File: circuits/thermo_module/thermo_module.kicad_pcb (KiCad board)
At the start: 2 copper layers, 32.4 x 39.4 mm, 16 parts, among them IC3 LM285Z-1.2, IC4 TMP36

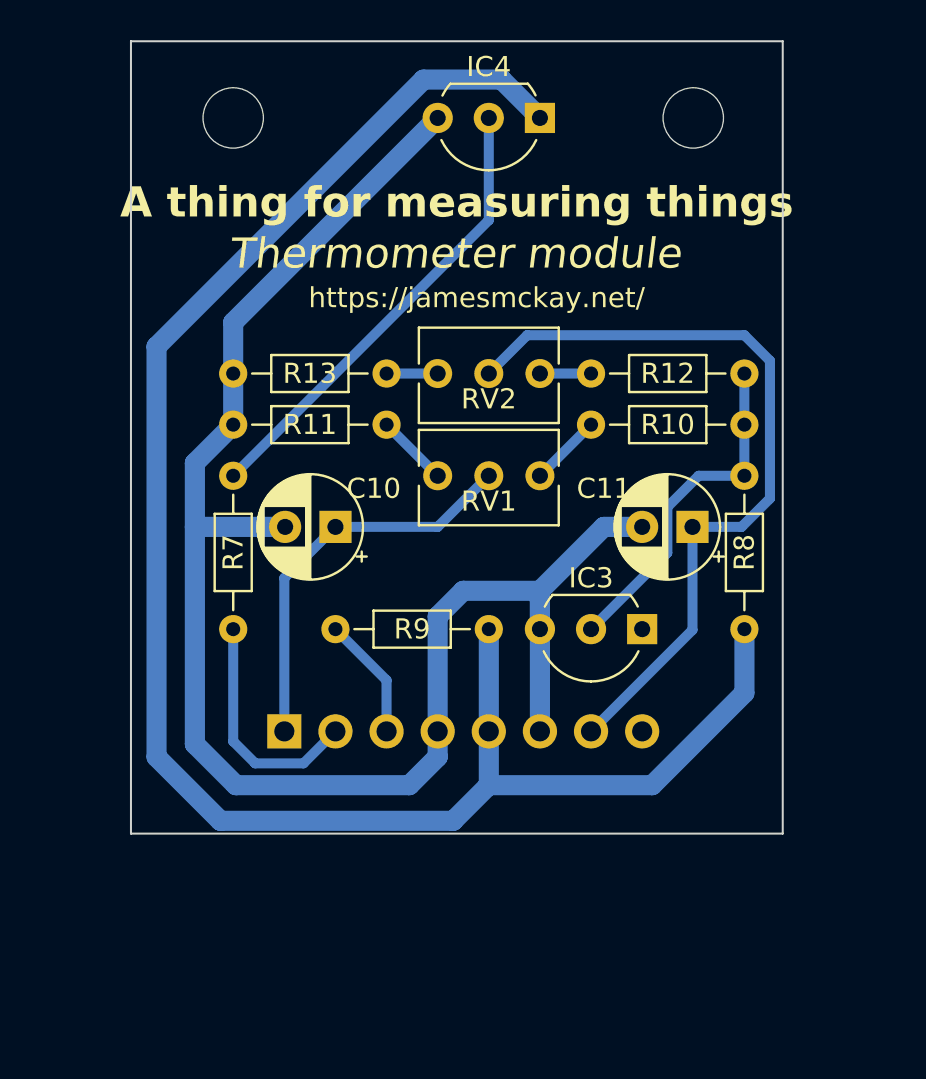
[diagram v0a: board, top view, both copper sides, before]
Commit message: Redesign thermo module to make it work
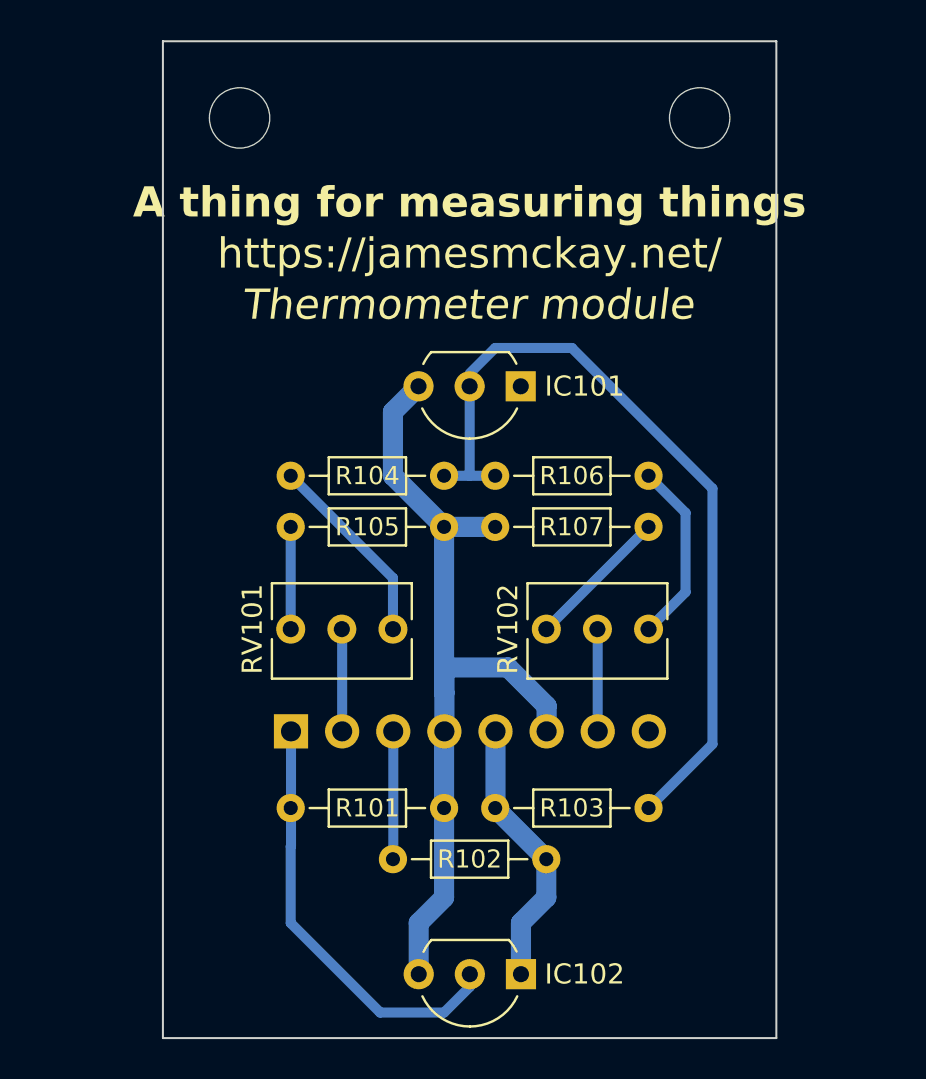
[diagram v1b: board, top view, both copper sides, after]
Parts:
- removed C10, C11: 1uF, Capacitor_THT:CP_Radial_D5.0mm_P2.50mm
- removed J5: ~, Connector_PinHeader_2.54mm:PinHeader_1x08_P2.54mm_Vertical
- removed R7: 33k, Resistor_THT:R_Axial_DIN0204_L3.6mm_D1.6mm_P7.62mm_Horizontal
- added J101: ~, Connector_PinHeader_2.54mm:PinHeader_1x08_P2.54mm_Vertical, B.Cu at (144.2, 79.4)
- added R101: 47k, Resistor_THT:R_Axial_DIN0204_L3.6mm_D1.6mm_P7.62mm_Horizontal, F.Cu at (151.8, 83.2)
- R103: renamed from R8; value 150k -> 75k
- R104: renamed from R10; value 100k -> 51k
- R105: renamed from R11; value 68k -> 33k
- R106: renamed from R12; value 20k -> 10k
- R107: renamed from R13; value 100k -> 51k
- moved IC102 42.6 mm to (155.6, 91.4)
- moved R103 15.2 mm to (154.3, 83.2), turned to 0 degrees
- moved R104 15.1 mm to (151.8, 66.7)
- moved R107 15.1 mm to (161.9, 69.2)
- moved RV102 13.8 mm to (161.9, 74.3)
- moved IC101 13.5 mm to (155.6, 62.2)
- moved R106 13.4 mm to (154.3, 66.7), turned to 0 degrees
- moved R102 11.8 mm to (156.8, 85.7)
- moved RV101 10.6 mm to (149.2, 74.3)
- moved R105 6.96 mm to (144.1, 69.2), turned to 0 degrees
- moved REF** 0.32 mm to (141.6, 48.9)
- moved REF** 0.32 mm to (164.5, 48.9)
- renumbered IC3 to IC101, IC4 to IC102, R9 to R102, RV1 to RV101, RV2 to RV102
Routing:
- net Net-(IC102-+V_{S}): track 89.8 -> 13.6 mm
- net Net-(IC101-A): track 81.5 -> 42.2 mm
- net Net-(J101-Pin_7): track 38.8 -> 5.06 mm
- net Net-(IC101-K): track 16.9 -> 39.7 mm
- net Net-(J101-Pin_2): track 19.9 -> 5.06 mm
- net Net-(J5-Pin_2): track 11.8 -> 0.00 mm
- net Net-(R106-Pad2): track 2.54 -> 9.14 mm
- net Net-(R104-Pad2): track 3.59 -> 9.72 mm
- net Net-(R107-Pad1): track 2.54 -> 7.18 mm
- net Net-(IC102-V_{OUT}): track 23.0 -> 21.4 mm
- net Net-(R105-Pad1): track 3.59 -> 5.08 mm
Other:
- board size 32.4 x 39.4 mm -> 30.5 x 49.5 mm

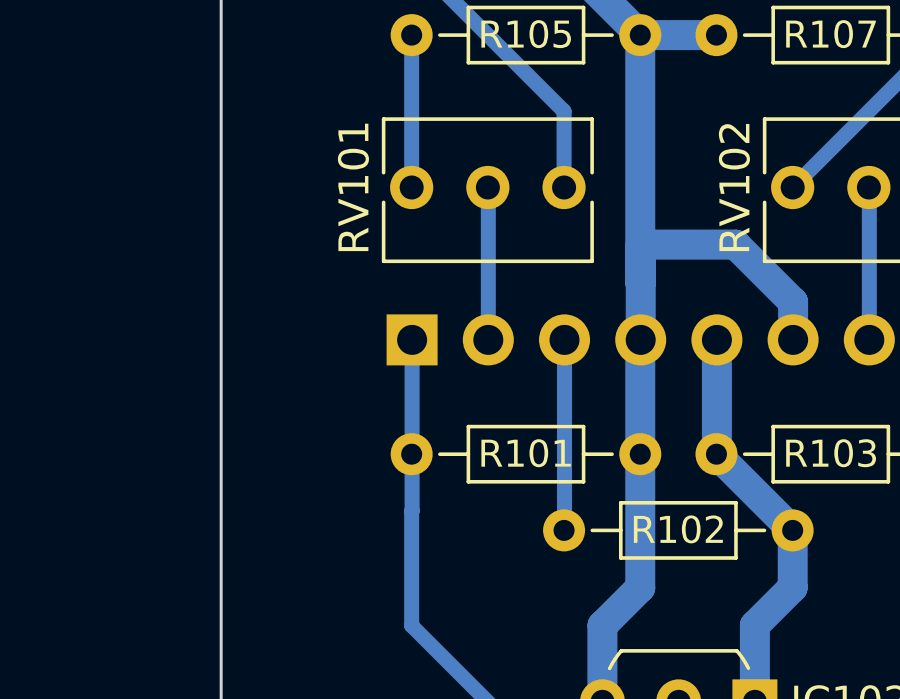
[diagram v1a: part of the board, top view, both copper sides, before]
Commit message: Fix for input pins the wrong way round
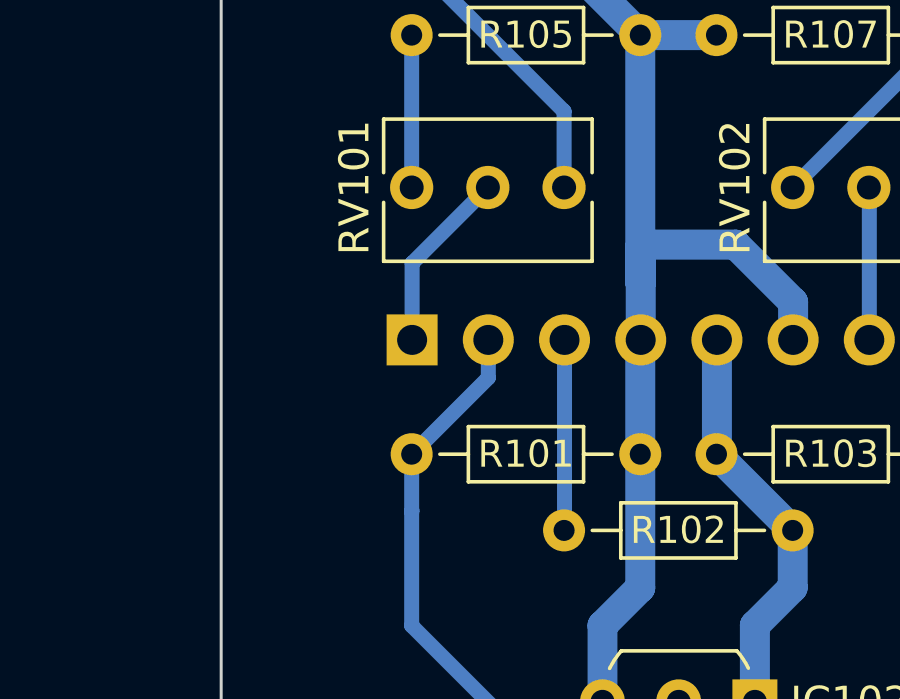
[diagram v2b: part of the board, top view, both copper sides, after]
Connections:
- J101 pad 1: Net-(IC102-V_{OUT}) -> Net-(J101-Pin_1)
- J101 pad 2: Net-(J101-Pin_2) -> Net-(IC102-V_{OUT})
- RV101 pad 2: Net-(J101-Pin_2) -> Net-(J101-Pin_1)
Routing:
- net Net-(J101-Pin_1): track 0.00 -> 6.13 mm
- net Net-(J101-Pin_2): track 5.06 -> 0.00 mm
- net Net-(IC102-V_{OUT}): track 21.4 -> 22.5 mm
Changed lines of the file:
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@@
       (disableapertmacros false)
       (usegerberextensions true)
-      (usegerberattributes true)
-      (usegerberadvancedattributes true)
+      (usegerberattributes false)
+      (usegerberadvancedattributes false)
       (creategerberjobfile false)
       (dashed_line_dash_ratio 12.000000)
@@
       (psa4output false)
       (plotreference true)
-      (plotvalue true)
+      (plotvalue false)
       (plotinvisibletext false)
       (sketchpadsonfab false)
@@
   (net 3 "Net-(IC102-+V_{S})")
   (net 4 "Net-(IC102-V_{OUT})")
-  (net 5 "Net-(J101-Pin_2)")
+  (net 5 "Net-(J101-Pin_1)")
   (net 6 "Net-(J101-Pin_3)")
   (net 7 "Net-(J101-Pin_7)")
@@
       (net 9 "Net-(R104-Pad2)") (pinfunction "1") (pintype "passive"))
     (pad "2" thru_hole circle (at -2.54 0) (size 1.44 1.44) (drill 0.8) (layers "*.Cu" "*.Mask")
-      (net 5 "Net-(J101-Pin_2)") (pinfunction "2") (pintype "passive"))
+      (net 5 "Net-(J101-Pin_1)") (pinfunction "2") (pintype "passive"))
     (pad "3" thru_hole circle (at -5.08 0) (size 1.44 1.44) (drill 0.8) (layers "*.Cu" "*.Mask")
       (net 10 "Net-(R105-Pad1)") (pinfunction "3") (pintype "passive"))
@@
       (stroke (width 0.1) (type solid)) (layer "B.Fab"))
     (pad "1" thru_hole rect (at 0 0 270) (size 1.7 1.7) (drill 1) (layers "*.Cu" "*.Mask")
-      (net 4 "Net-(IC102-V_{OUT})") (pinfunction "Pin_1") (pintype "passive"))
+      (net 5 "Net-(J101-Pin_1)") (pinfunction "Pin_1") (pintype "passive"))
     (pad "2" thru_hole oval (at 0 -2.54 270) (size 1.7 1.7) (drill 1) (layers "*.Cu" "*.Mask")
-      (net 5 "Net-(J101-Pin_2)") (pinfunction "Pin_2") (pintype "passive"))
+      (net 4 "Net-(IC102-V_{OUT})") (pinfunction "Pin_2") (pintype "passive"))
     (pad "3" thru_hole oval (at 0 -5.08 270) (size 1.7 1.7) (drill 1) (layers "*.Cu" "*.Mask")
       (net 6 "Net-(J101-Pin_3)") (pinfunction "Pin_3") (pintype "passive"))
@@
   (segment (start 155.585 91.44) (end 155.585 88.89) (width 1) (layer "B.Cu") (net 3))
   (segment (start 156.845 87.63) (end 156.845 85.725) (width 1) (layer "B.Cu") (net 3))
+  (segment (start 144.145 85.09) (end 144.145 83.185) (width 0.5) (layer "B.Cu") (net 4))
+  (segment (start 146.7 80.6375) (end 146.7 79.375) (width 0.5) (layer "B.Cu") (net 4))
   (segment (start 144.145 88.9) (end 148.59 93.345) (width 0.5) (layer "B.Cu") (net 4))
   (segment (start 144.16 85.075) (end 144.145 85.09) (width 0.5) (layer "B.Cu") (net 4))
   (segment (start 151.765 93.345) (end 153.045 92.065) (width 0.5) (layer "B.Cu") (net 4))
-  (segment (start 144.16 79.375) (end 144.16 85.075) (width 0.5) (layer "B.Cu") (net 4))
   (segment (start 148.59 93.345) (end 151.765 93.345) (width 0.5) (layer "B.Cu") (net 4))
+  (segment (start 144.1525 83.185) (end 146.7 80.6375) (width 0.5) (layer "B.Cu") (net 4))
   (segment (start 144.145 85.09) (end 144.145 88.9) (width 0.5) (layer "B.Cu") (net 4))
   (segment (start 153.045 92.065) (end 153.045 91.43) (width 0.5) (layer "B.Cu") (net 4))
-  (segment (start 146.7 79.375) (end 146.7 74.31) (width 0.5) (layer "B.Cu") (net 5))
+  (segment (start 144.145 83.185) (end 144.1525 83.185) (width 0.5) (layer "B.Cu") (net 4))
+  (segment (start 144.16 79.375) (end 144.16 76.82) (width 0.5) (layer "B.Cu") (net 5))
+  (segment (start 144.16 76.82) (end 146.685 74.295) (width 0.5) (layer "B.Cu") (net 5))
   (segment (start 149.24 85.71) (end 149.24 79.375) (width 0.5) (layer "B.Cu") (net 6))
   (segment (start 159.4 79.375) (end 159.4 74.31) (width 0.5) (layer "B.Cu") (net 7))
